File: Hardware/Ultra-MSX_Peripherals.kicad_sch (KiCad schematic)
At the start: 56 parts, among them J4 OST_Conn_302-S341, J5 Amphenol_L17H1220134, J6 DIN-8_SDF-80J, J7 AdamTech_USB3-2_USB_C_Recepta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, J8 SDF-130J, J9 Ultra-av-daughter, Q2 MMBT2907AM3T5G, U16 LM211

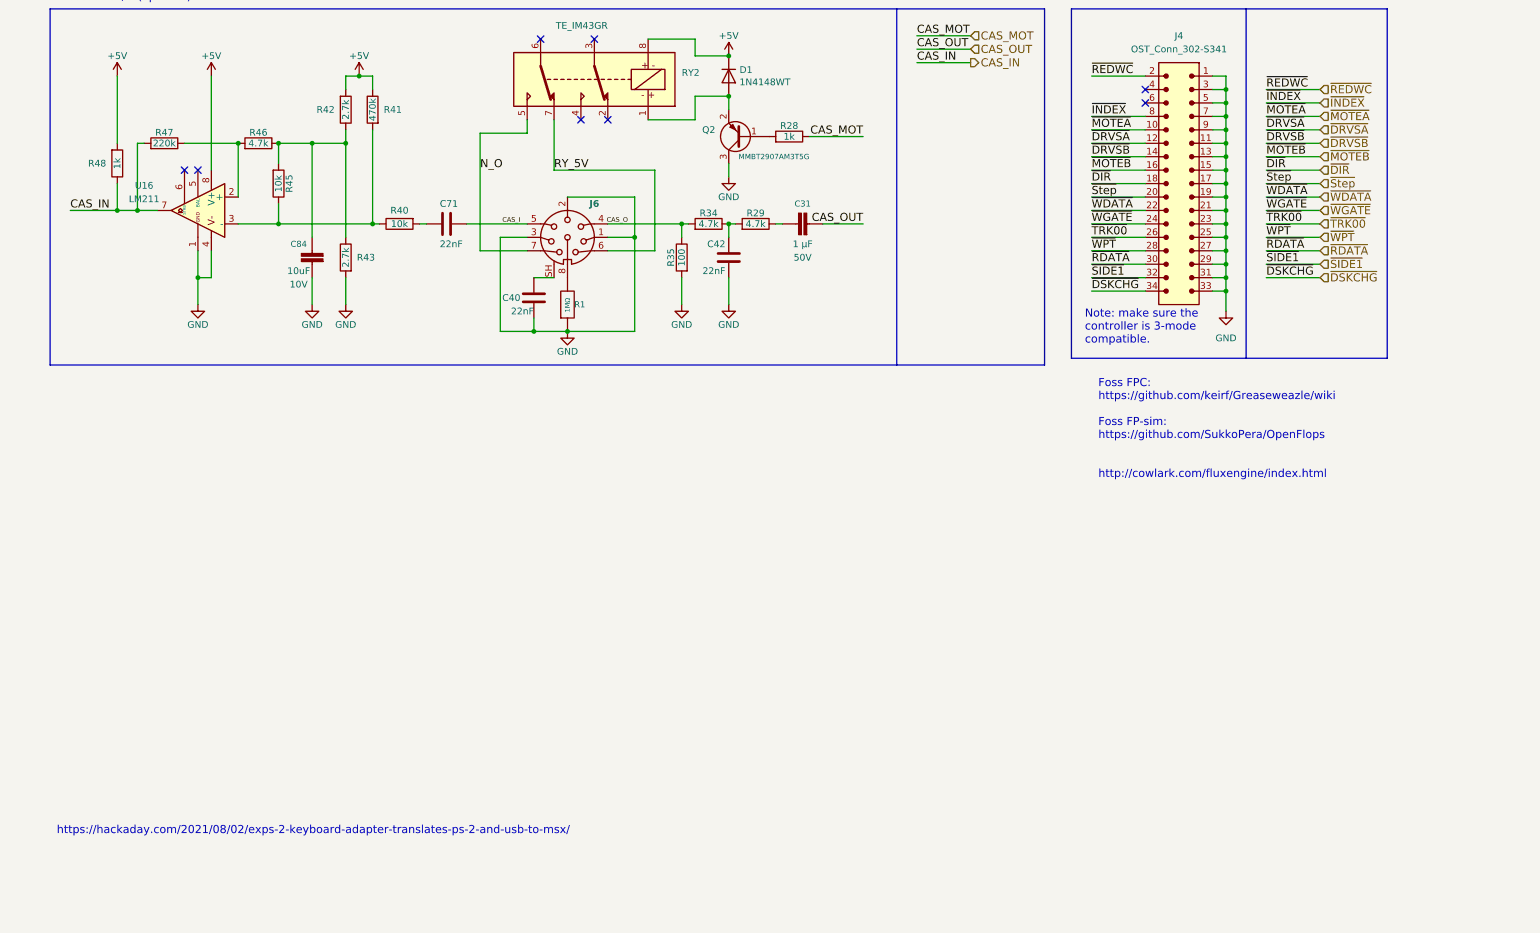
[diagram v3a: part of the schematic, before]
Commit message: Added SD-card slot, made basic 3d-model for sd-card slot, connected it up in the schematic, and numerous other tweaks.
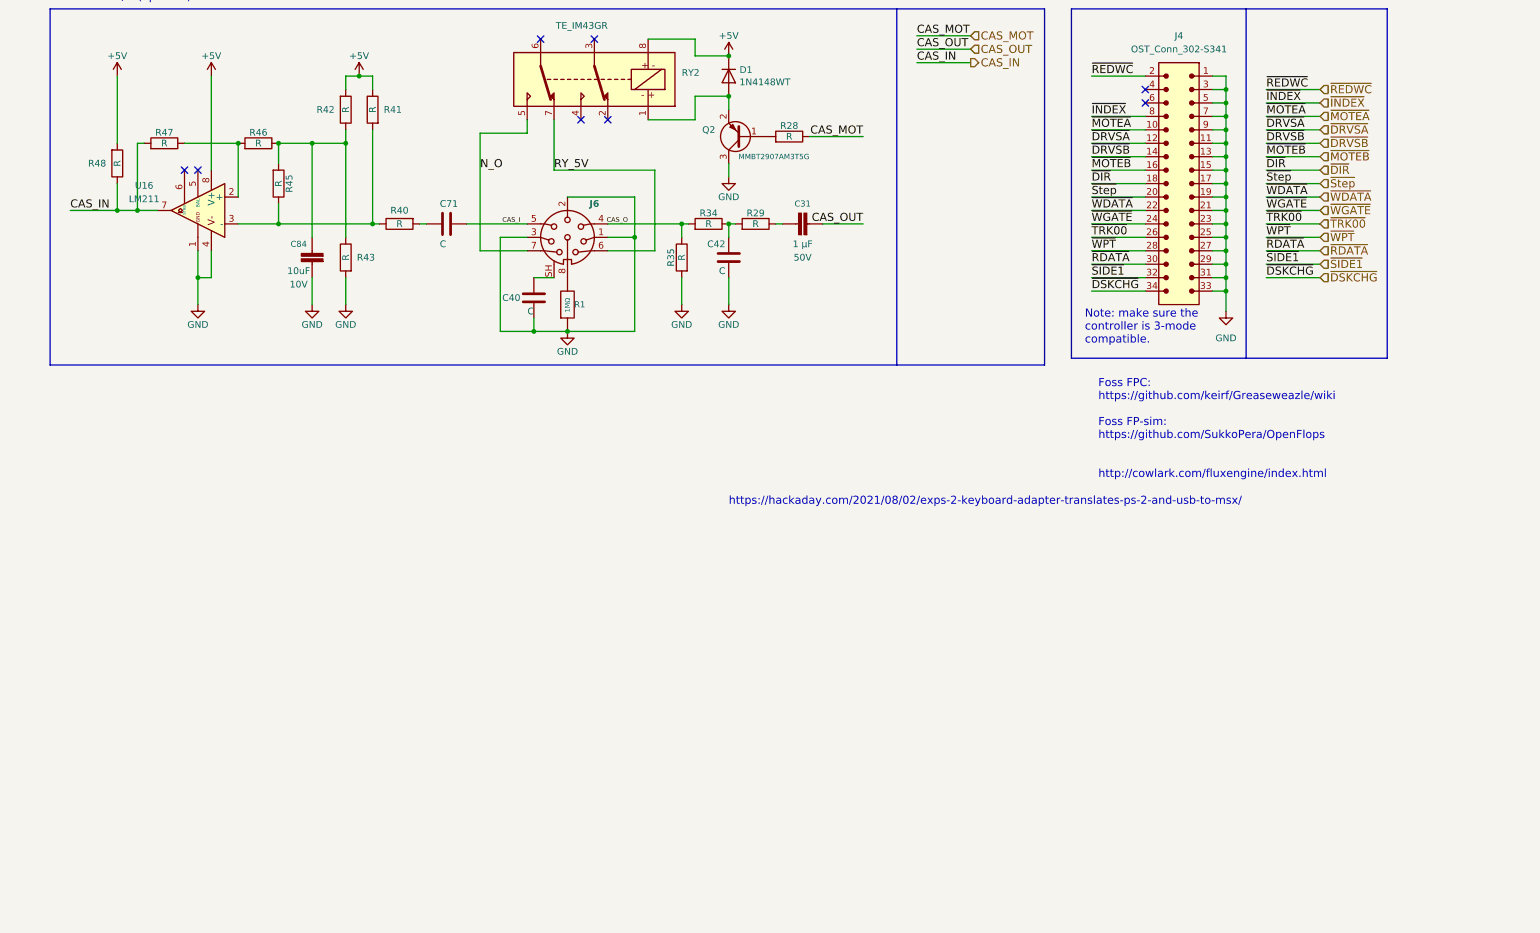
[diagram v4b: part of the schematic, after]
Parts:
- C40, C42, C71: value 22nF -> C
- R28, R48: value 1k -> R
- R29, R34, R46: value 4.7k -> R
- R35: value 100 -> R
- R40, R45: value 10k -> R
- R41: value 470k -> R
- R42, R43: value 2.7k -> R
- R47: value 220k -> R
- RY2: Manufacturer_Name TE Connectivity -> (none); Manufacturer_Part_Number IM43GR -> (none); Mouser Part Number 655-IM43GR -> (none); Mouser Price/Stock https://www.mouser.co.uk/ProductDetail/TE-Connectivity-PB/I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 -> (none)
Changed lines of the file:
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@@
   )
   (text "https://hackaday.com/2021/08/02/exps-2-keyboard-adapter-translates-ps-2-and-usb-to-msx/"
-    (at 19.05 251.46 0)
+    (at 146.05 189.23 0)
     (effects (font (size 1.524 1.524)) (justify left bottom))
   )
@@
     (in_bom yes) (on_board yes)
     (property "Reference" "R48" (id 0) (at 26.67 124.46 0))
-    (property "Value" "1k" (id 1) (at 30.48 124.46 90))
+    (property "Value" "R" (id 1) (at 30.48 124.46 90))
     (property "Footprint" "Resistor_SMD:R_0603_1608Metric" (id 2) (at 28.702 124.46 90)
       (effects (font (size 1.27 1.27)) hide)
@@
       (effects (font (size 1.27 1.27)) (justify left))
     )
-    (property "Value" "22nF" (id 1) (at 91.44 139.7 90)
+    (property "Value" "C" (id 1) (at 91.44 139.7 90)
       (effects (font (size 1.27 1.27)) (justify left))
     )
@@
     (in_bom yes) (on_board yes)
     (property "Reference" "R40" (id 0) (at 83.82 133.35 90))
-    (property "Value" "10k" (id 1) (at 83.82 135.89 90))
+    (property "Value" "R" (id 1) (at 83.82 135.89 90))
     (property "Footprint" "Resistor_SMD:R_0603_1608Metric" (id 2) (at 83.82 134.112 90)
       (effects (font (size 1.27 1.27)) hide)
@@
     (in_bom yes) (on_board yes)
     (property "Reference" "R41" (id 0) (at 82.55 114.3 0))
-    (property "Value" "470k" (id 1) (at 78.74 114.3 90))
+    (property "Value" "R" (id 1) (at 78.74 114.3 90))
     (property "Footprint" "Resistor_SMD:R_0603_1608Metric" (id 2) (at 80.518 114.3 90)
       (effects (font (size 1.27 1.27)) hide)
@@
     (in_bom yes) (on_board yes)
     (property "Reference" "R47" (id 0) (at 39.37 118.618 90))
-    (property "Value" "220k" (id 1) (at 39.37 120.65 90))
+    (property "Value" "R" (id 1) (at 39.37 120.65 90))
     (property "Footprint" "Resistor_SMD:R_0805_2012Metric" (id 2) (at 39.37 122.428 90)
       (effects (font (size 1.27 1.27)) hide)
@@
     (in_bom yes) (on_board yes)
     (property "Reference" "R46" (id 0) (at 57.15 118.618 90))
-    (property "Value" "4.7k" (id 1) (at 57.15 120.65 90))
+    (property "Value" "R" (id 1) (at 57.15 120.65 90))
     (property "Footprint" "Resistor_SMD:R_0603_1608Metric" (id 2) (at 57.15 122.428 90)
       (effects (font (size 1.27 1.27)) hide)
@@
     (in_bom yes) (on_board yes)
     (property "Reference" "R45" (id 0) (at 62.992 128.27 90))
-    (property "Value" "10k" (id 1) (at 60.96 128.27 90))
+    (property "Value" "R" (id 1) (at 60.96 128.27 90))
     (property "Footprint" "Resistor_SMD:R_0603_1608Metric" (id 2) (at 59.182 128.27 90)
       (effects (font (size 1.27 1.27)) hide)
@@
     (in_bom yes) (on_board yes)
     (property "Reference" "R42" (id 0) (at 69.85 114.3 0))
-    (property "Value" "2.7k" (id 1) (at 73.66 114.3 90))
+    (property "Value" "R" (id 1) (at 73.66 114.3 90))
     (property "Footprint" "Resistor_SMD:R_0603_1608Metric" (id 2) (at 71.882 114.3 90)
       (effects (font (size 1.27 1.27)) hide)
@@
     (in_bom yes) (on_board yes)
     (property "Reference" "R43" (id 0) (at 77.47 142.24 0))
-    (property "Value" "2.7k" (id 1) (at 73.66 142.24 90))
+    (property "Value" "R" (id 1) (at 73.66 142.24 90))
     (property "Footprint" "Resistor_SMD:R_0603_1608Metric" (id 2) (at 75.438 142.24 90)
       (effects (font (size 1.27 1.27)) hide)
@@
     (in_bom yes) (on_board yes)
     (property "Reference" "R35" (id 0) (at 135.128 142.24 90))
-    (property "Value" "100" (id 1) (at 137.16 142.24 90))
+    (property "Value" "R" (id 1) (at 137.16 142.24 90))
     (property "Footprint" "Resistor_SMD:R_0603_1608Metric" (id 2) (at 138.938 142.24 90)
       (effects (font (size 1.27 1.27)) hide)
@@
     (in_bom yes) (on_board yes)
     (property "Reference" "R34" (id 0) (at 142.24 133.858 90))
-    (property "Value" "4.7k" (id 1) (at 142.24 135.89 90))
+    (property "Value" "R" (id 1) (at 142.24 135.89 90))
     (property "Footprint" "Resistor_SMD:R_0603_1608Metric" (id 2) (at 142.24 137.668 90)
       (effects (font (size 1.27 1.27)) hide)
@@
     (in_bom yes) (on_board yes)
     (property "Reference" "R29" (id 0) (at 151.13 133.858 90))
-    (property "Value" "4.7k" (id 1) (at 151.13 135.89 90))
+    (property "Value" "R" (id 1) (at 151.13 135.89 90))
     (property "Footprint" "Resistor_SMD:R_0603_1608Metric" (id 2) (at 151.13 137.668 90)
       (effects (font (size 1.27 1.27)) hide)
@@
       (effects (font (size 1.27 1.27)) (justify left))
     )
-    (property "Value" "22nF" (id 1) (at 145.415 144.78 0)
+    (property "Value" "C" (id 1) (at 145.415 144.78 0)
       (effects (font (size 1.27 1.27)) (justify left))
     )
@@
     (in_bom yes) (on_board yes)
     (property "Reference" "R28" (id 0) (at 157.48 117.348 90))
-    (property "Value" "1k" (id 1) (at 157.48 119.38 90))
+    (property "Value" "R" (id 1) (at 157.48 119.38 90))
     (property "Footprint" "Resistor_SMD:R_0603_1608Metric" (id 2) (at 157.48 121.158 90)
       (effects (font (size 1.27 1.27)) hide)
@@
       (effects (font (size 1.27 1.27)) (justify left) hide)
     )
-    (property "Height" "" (id 5) (at 114.3 106.045 0)
-      (effects (font (size 1.27 1.27)) (justify left) hide)
-    )
-    (property "Mouser Part Number" "655-IM43GR" (id 6) (at 104.14 103.505 0)
-      (effects (font (size 1.27 1.27)) (justify left) hide)
-    )
-    (property "Mouser Price/Stock" "https://www.mouser.co.uk/ProductDetail/TE-Connectivity-PB/IM43GR?qs=8DUeuUvkWiGcTCpHR6BP%2FQ%3D%3D" (id 7) (at 93.98 98.425 0)
-      (effects (font (size 1.27 1.27)) (justify left) hide)
-    )
-    (property "Manufacturer_Name" "TE Connectivity" (id 8) (at 104.14 98.425 0)
-      (effects (font (size 1.27 1.27)) (justify left) hide)
-    )
-    (property "Manufacturer_Part_Number" "IM43GR" (id 9) (at 104.14 95.885 0)
-      (effects (font (size 1.27 1.27)) (justify left) hide)
-    )
     (property "Manufacturer" "TE Connectivity" (id 10) (at 104.14 123.825 0)
       (effects (font (size 1.27 1.27)) (justify left) hide)
@@
       (effects (font (size 1.27 1.27)) (justify left))
     )
-    (property "Value" "22nF" (id 1) (at 109.22 152.4 0)
+    (property "Value" "C" (id 1) (at 109.22 152.4 0)
       (effects (font (size 1.27 1.27)) (justify left))
     )

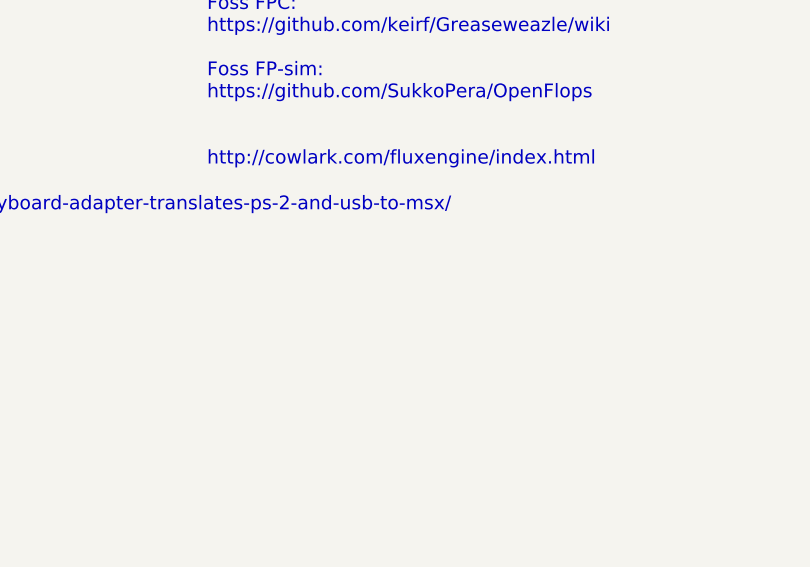
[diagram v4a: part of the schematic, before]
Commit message: Redesigned VDP-board to include a socket, increased it to 4 layers. Various clean-ups here and there. Improved the printer-port and joystick-port 3D-models. Improved the cooling-fin 3D-model, and added attachment-spring in 3D-model.
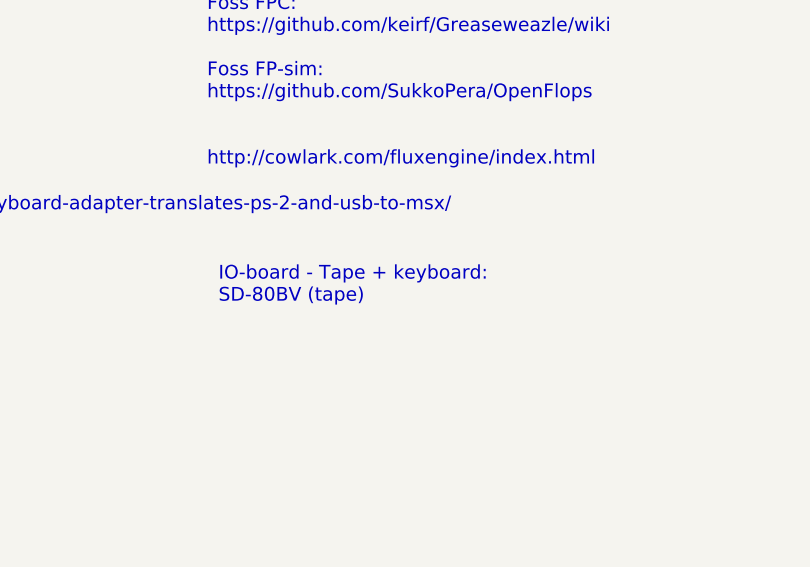
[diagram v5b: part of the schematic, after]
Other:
- note added: "IO-board - Tape + keyboard: SD-80BV (tape)"
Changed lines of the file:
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@@
+    (effects (font (size 1.524 1.524)) (justify left bottom))
+  )
+  (text "IO-board - Tape + keyboard:\nSD-80BV (tape)\n" (at 217.17 199.39 0)
     (effects (font (size 1.524 1.524)) (justify left bottom))
   )
@@
       (effects (font (size 1.27 1.27)) hide)
     )
-    (property "Datasheet" "https://www.amphenolcanada.com/ProductSearch/Pdf/DSUB_CAT.pdf#Page=67" (id 3) (at 288.29 57.15 0)
-      (effects (font (size 1.27 1.27)) hide)
-    )
+    (property "Datasheet" "https://cdn.amphenol-cs.com/media/wysiwyg/files/documentation/datasheet/inputoutput/l17h_stacked_dsub.pdf" (id 3) (at 288.29 57.15 0)
+      (effects (font (size 1.27 1.27)) hide)
+    )
